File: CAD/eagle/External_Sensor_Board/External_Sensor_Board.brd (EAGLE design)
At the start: 50.8 x 43.4 mm, 14 parts, among them J1 SFW15R_FFC, J2 J30J-25, U1 MAX31725MTA+, U2 SSCMNNN015PA2A3, U3 P82B715

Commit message: Final layouts and gerbers
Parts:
- added U$1: SSL.3IN_SILK, images:SSL_SILK_.3IN
- added U$2: STAR, images:STAR_.3IN
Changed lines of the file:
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@@
 <?xml version="1.0" encoding="utf-8"?>
 <!DOCTYPE eagle SYSTEM "eagle.dtd">
-<eagle version="7.7.0">
+<eagle version="6.5.0">
 <drawing>
 <settings>
@@
 <layer number="2" name="Route2" color="1" fill="3" visible="no" active="yes"/>
 <layer number="3" name="Route3" color="4" fill="3" visible="no" active="yes"/>
+<layer number="4" name="Route4" color="1" fill="4" visible="no" active="yes"/>
+<layer number="5" name="Route5" color="4" fill="4" visible="no" active="yes"/>
+<layer number="6" name="Route6" color="1" fill="8" visible="no" active="yes"/>
+<layer number="7" name="Route7" color="4" fill="8" visible="no" active="yes"/>
+<layer number="8" name="Route8" color="1" fill="2" visible="no" active="yes"/>
+<layer number="9" name="Route9" color="4" fill="2" visible="no" active="yes"/>
+<layer number="10" name="Route10" color="1" fill="7" visible="no" active="yes"/>
+<layer number="11" name="Route11" color="4" fill="7" visible="no" active="yes"/>
+<layer number="12" name="Route12" color="1" fill="5" visible="no" active="yes"/>
+<layer number="13" name="Route13" color="4" fill="5" visible="no" active="yes"/>
 <layer number="14" name="Route14" color="1" fill="6" visible="no" active="yes"/>
 <layer number="15" name="Route15" color="4" fill="6" visible="no" active="yes"/>
@@
 <pass name="Default">
 <param name="RoutingGrid" value="50mil"/>
-<param name="AutoGrid" value="1"/>
-<param name="Efforts" value="0"/>
-<param name="TopRouterVariant" value="1"/>
 <param name="tpViaShape" value="round"/>
-<param name="PrefDir.1" value="a"/>
+<param name="PrefDir.1" value="|"/>
 <param name="PrefDir.2" value="0"/>
 <param name="PrefDir.3" value="0"/>
@@
 <param name="PrefDir.14" value="0"/>
 <param name="PrefDir.15" value="0"/>
-<param name="PrefDir.16" value="a"/>
+<param name="PrefDir.16" value="-"/>
 <param name="cfVia" value="8"/>
 <param name="cfNonPref" value="5"/>
@@
 <attribute name="NAME" x="2.0828" y="35.4584" size="0.8128" layer="25"/>
 </element>
+<element name="U$1" library="images" package="SSL_SILK_.3IN" value="SSL.3IN_SILK" x="46.99" y="5.08" rot="MR0"/>
+<element name="U$2" library="images" package="STAR_.3IN" value="STAR" x="11.43" y="5.08" rot="MR0"/>
 </elements>
 <signals>

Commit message: Beginning rework of expternal sensor board.
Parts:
- removed C2: 1uF, resistor:C0603
- removed C3: 100nF, resistor:C0603
- removed U3: P82B715, CM_IC:SO8
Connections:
- removed net SCL_BUFF: J2.25, U3.2
- removed net SDA_BUFF: J2.23, U3.7
- net +3V3: no longer C2.1, C3.1, U3.8
- net GND: no longer C2.2, C3.2, U3.4
- net SCL: now also J2.25; no longer U3.3
- net SDA: now also J2.23; no longer U3.6
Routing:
- net CAM_D0_P: track 57.9 -> 0.00 mm, vias 2 -> 0
- net CAM_D1_P: track 56.8 -> 0.00 mm, vias 1 -> 0
- net CAM_D0_N: track 56.2 -> 0.00 mm, vias 2 -> 0
- net CAM_D1_N: track 54.4 -> 0.00 mm, vias 1 -> 0
- net SDA_BUFF: track 53.5 -> 0.00 mm, vias 2 -> 0
- net SCL_BUFF: track 49.0 -> 0.00 mm, vias 2 -> 0
- net CAM_GND4: track 47.9 -> 0.00 mm, vias 1 -> 0
- net CAM_GPIO0: track 46.6 -> 0.00 mm, vias 1 -> 0
- net CAM_GPIO1: track 45.7 -> 0.00 mm, vias 1 -> 0
- net CAM_SCL: track 42.9 -> 0.00 mm, vias 1 -> 0
- net CAM_GND3: track 42.3 -> 0.00 mm, vias 1 -> 0
- net CAM_GND1: track 41.4 -> 0.00 mm, vias 1 -> 0
- net CAM_GND2: track 36.7 -> 0.00 mm, vias 1 -> 0
- net SDA: track 79.1 -> 113.4 mm
- net SCL: track 80.3 -> 108.9 mm
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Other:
- outline, holes or cut-outs redrawn
- board text added: "OPTIONAL"
- board text added: "REV 2 May 2017"
- board text removed: "REV 1.1 Feb. 2017"

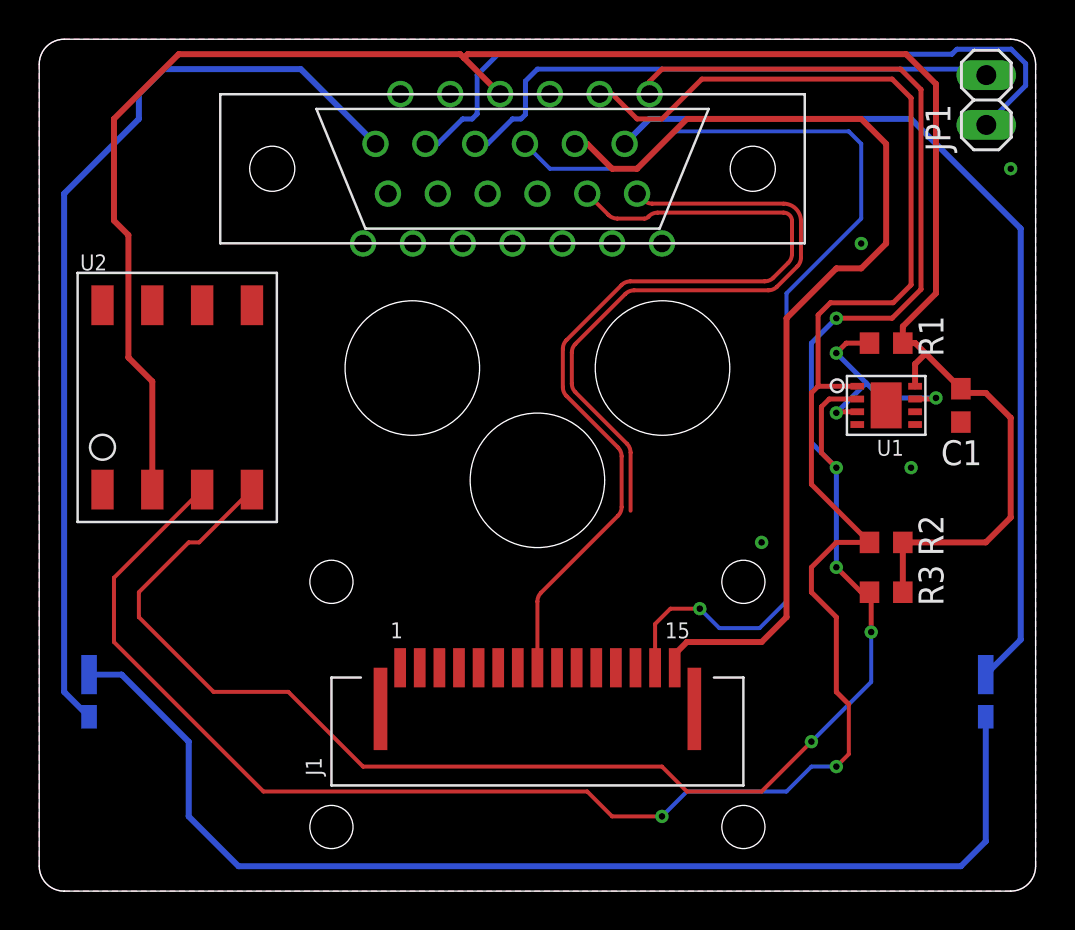
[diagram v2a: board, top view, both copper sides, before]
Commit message: Finished External Sensor Board reroute.
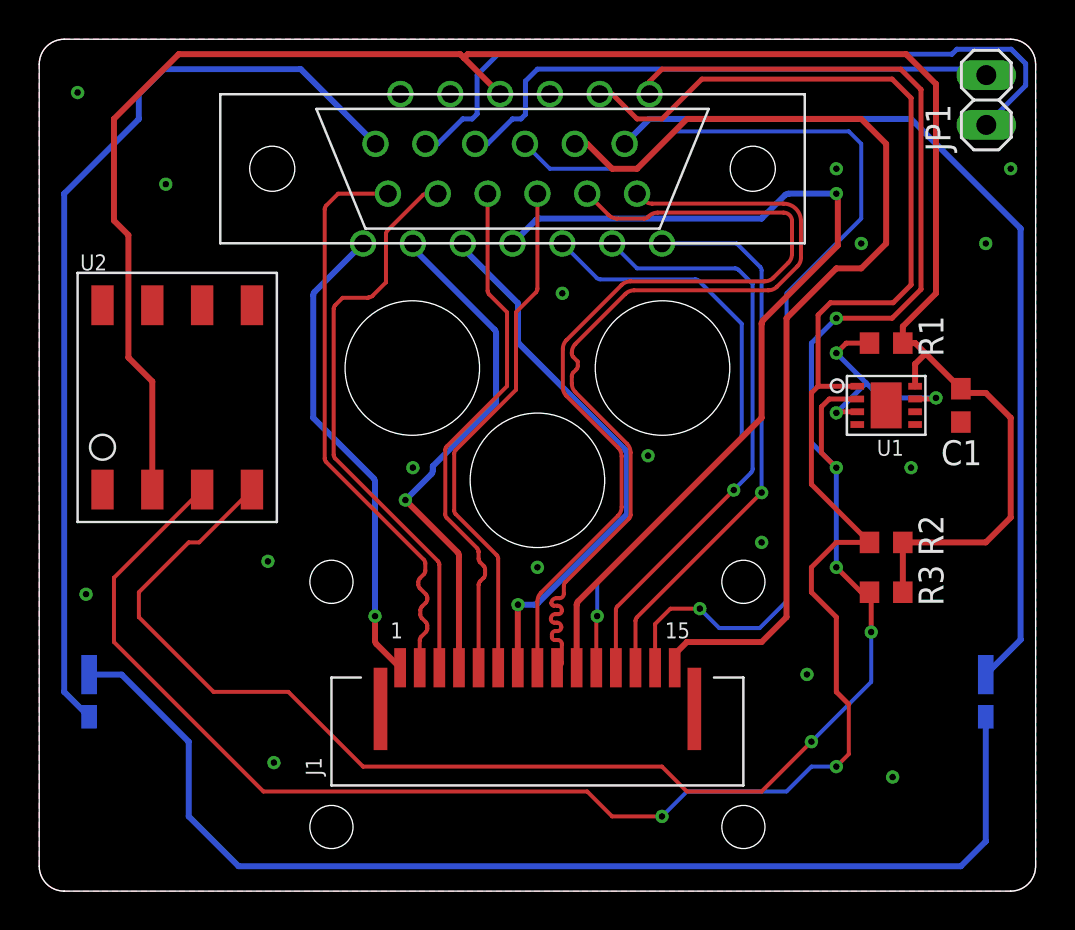
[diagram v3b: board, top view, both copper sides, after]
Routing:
- net CAM_GND4: track 0.00 -> 47.2 mm, vias 0 -> 1
- net CAM_GPIO0: track 0.00 -> 31.4 mm, vias 0 -> 1
- net CAM_GPIO1: track 0.00 -> 30.4 mm, vias 0 -> 1
- net CAM_D0_P: track 0.00 -> 29.7 mm
- net CAM_D0_N: track 0.00 -> 29.7 mm
- net CAM_SCL: track 0.00 -> 28.6 mm, vias 0 -> 1
- net CAM_GND3: track 0.00 -> 27.9 mm, vias 0 -> 1
- net CAM_D1_P: track 0.00 -> 26.8 mm
- net CAM_D1_N: track 0.00 -> 26.7 mm
- net CAM_GND2: track 0.00 -> 26.4 mm, vias 0 -> 1
- net CAM_GND1: track 0.00 -> 24.5 mm, vias 0 -> 1
- net CAM_C_P: track 33.8 -> 45.4 mm

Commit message: Minor changes to external board upon review.
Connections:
- removed net CAM_GND1: J1.1, J2.1
- removed net CAM_GND2: J1.4, J2.3
- removed net CAM_GND3: J1.7, J2.5
- removed net CAM_GND4: J1.10, J2.7
- net GND: now also J1.1, J1.10, J1.4, J1.7, J2.1, J2.3, J2.5, J2.7
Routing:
- net CAM_GND4: track 47.2 -> 0.00 mm, vias 1 -> 0
- net CAM_GND3: track 27.9 -> 0.00 mm, vias 1 -> 0
- net CAM_GND2: track 26.4 -> 0.00 mm, vias 1 -> 0
- net CAM_GND1: track 24.5 -> 0.00 mm, vias 1 -> 0
- net CAM_GPIO0: track 31.4 -> 23.2 mm
- net CAM_D0_P: track 29.7 -> 30.8 mm
- net CAM_D0_N: track 29.7 -> 30.4 mm

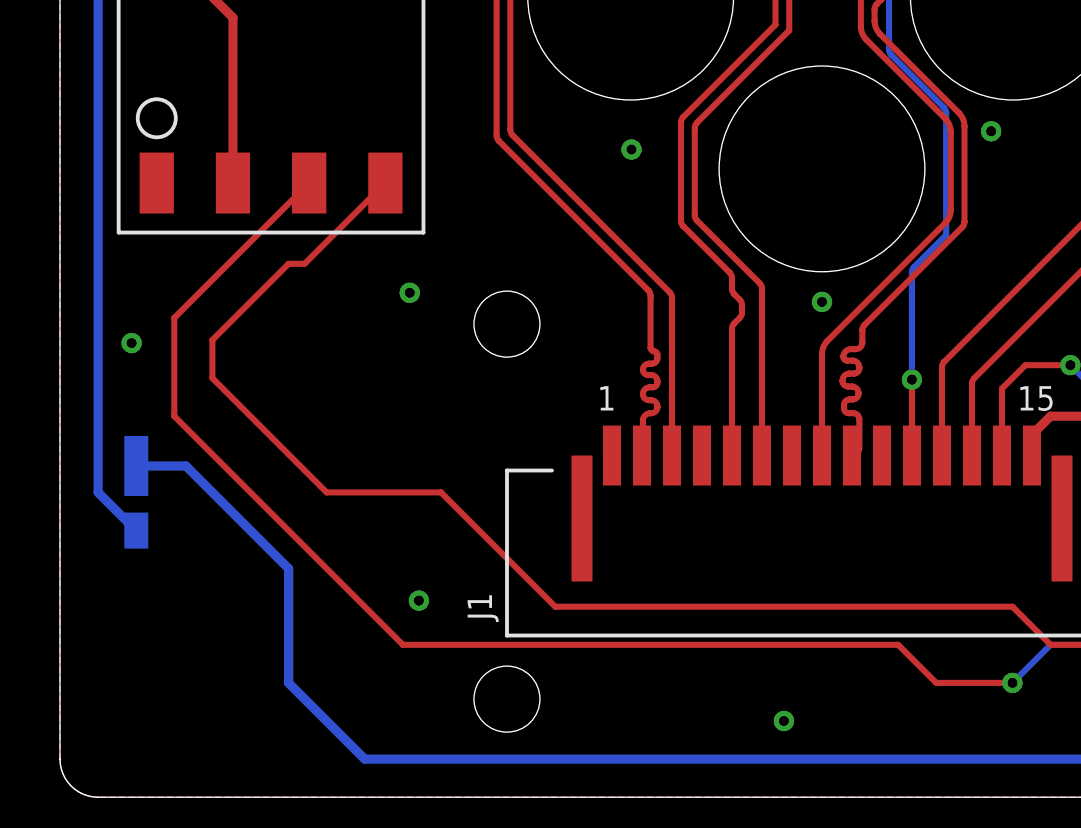
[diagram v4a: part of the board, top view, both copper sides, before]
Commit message: ESB traces and breakout 15 pin labels
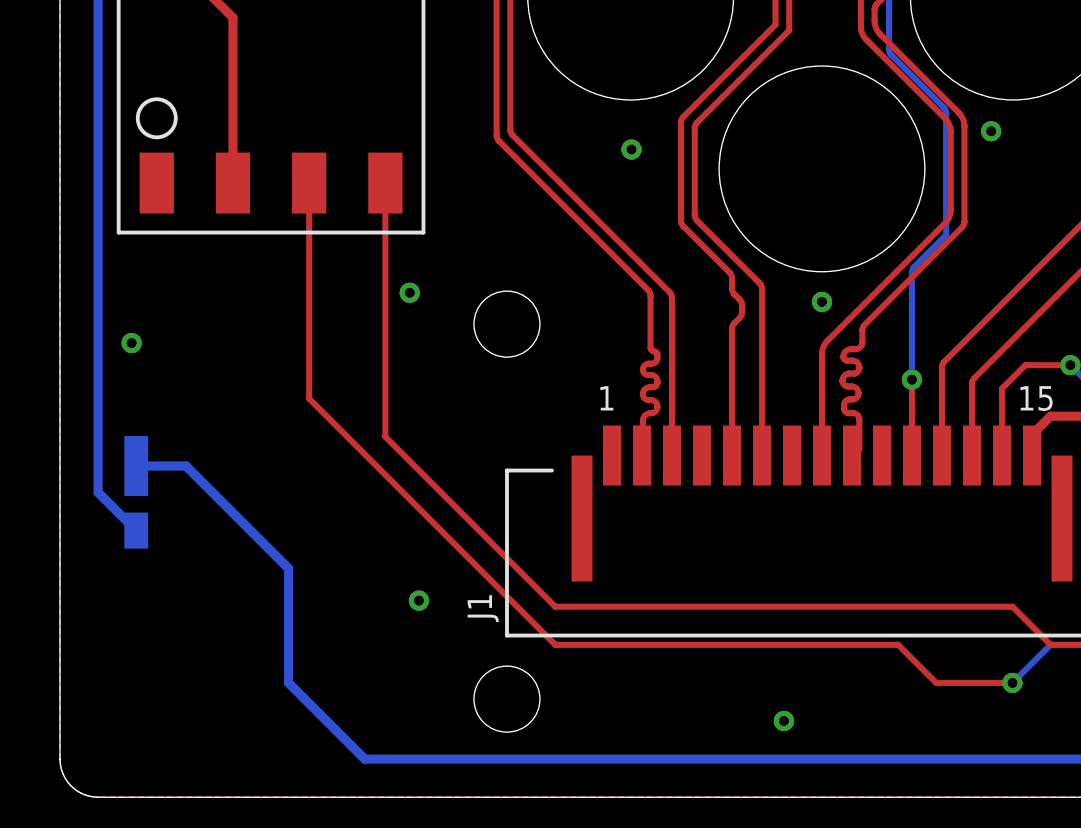
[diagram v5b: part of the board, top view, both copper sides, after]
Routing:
- net SCL: track 108.9 -> 101.6 mm
- net SDA: track 113.4 -> 106.7 mm
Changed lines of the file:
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@@
 <?xml version="1.0" encoding="utf-8"?>
 <!DOCTYPE eagle SYSTEM "eagle.dtd">
-<eagle version="7.7.0">
+<eagle version="6.5.0">
 <drawing>
 <settings>
@@
 <pass name="Default">
 <param name="RoutingGrid" value="50mil"/>
-<param name="AutoGrid" value="1"/>
-<param name="Efforts" value="0"/>
-<param name="TopRouterVariant" value="1"/>
 <param name="tpViaShape" value="round"/>
 <param name="PrefDir.1" value="|"/>
@@
 <wire x1="40.64" y1="21.59" x2="42.33" y2="21.59" width="0.254" layer="1"/>
 <contactref element="U2" pad="3"/>
-<wire x1="8.3058" y1="24.2824" x2="3.81" y2="19.7866" width="0.2032" layer="1"/>
-<wire x1="3.81" y1="19.7866" x2="3.81" y2="16.51" width="0.2032" layer="1"/>
-<wire x1="3.81" y1="16.51" x2="11.43" y2="8.89" width="0.2032" layer="1"/>
-<wire x1="11.43" y1="8.89" x2="27.94" y2="8.89" width="0.2032" layer="1"/>
 <wire x1="27.94" y1="8.89" x2="29.21" y2="7.62" width="0.2032" layer="1"/>
 <wire x1="29.21" y1="7.62" x2="31.75" y2="7.62" width="0.2032" layer="1"/>
@@
 <wire x1="44.45" y1="44.2468" x2="43.4848" y2="45.212" width="0.254" layer="1"/>
 <wire x1="43.4848" y1="45.212" x2="33.782" y2="45.212" width="0.254" layer="1"/>
+<wire x1="27.94" y1="8.89" x2="16.51" y2="8.89" width="0.2032" layer="1"/>
+<wire x1="16.51" y1="8.89" x2="8.3058" y2="17.0942" width="0.2032" layer="1"/>
+<wire x1="8.3058" y1="17.0942" x2="8.3058" y2="24.2824" width="0.2032" layer="1"/>
 </signal>
 <signal name="SCL">
@@
 <wire x1="42.418" y1="18.962" x2="42.33" y2="19.05" width="0.254" layer="1"/>
 <contactref element="U2" pad="4"/>
-<wire x1="10.8458" y1="24.2824" x2="8.1534" y2="21.59" width="0.2032" layer="1"/>
-<wire x1="8.1534" y1="21.59" x2="7.62" y2="21.59" width="0.2032" layer="1"/>
-<wire x1="7.62" y1="21.59" x2="5.08" y2="19.05" width="0.2032" layer="1"/>
-<wire x1="5.08" y1="19.05" x2="5.08" y2="17.78" width="0.2032" layer="1"/>
-<wire x1="5.08" y1="17.78" x2="8.89" y2="13.97" width="0.2032" layer="1"/>
-<wire x1="8.89" y1="13.97" x2="12.7" y2="13.97" width="0.2032" layer="1"/>
-<wire x1="12.7" y1="13.97" x2="16.51" y2="10.16" width="0.2032" layer="1"/>
+<wire x1="10.8458" y1="15.8242" x2="16.51" y2="10.16" width="0.2032" layer="1"/>
 <wire x1="16.51" y1="10.16" x2="31.75" y2="10.16" width="0.2032" layer="1"/>
 <wire x1="31.75" y1="10.16" x2="33.02" y2="8.89" width="0.2032" layer="1"/>
@@
 <wire x1="39.37" y1="11.43" x2="42.418" y2="14.478" width="0.2032" layer="16"/>
 <wire x1="42.418" y1="14.478" x2="42.418" y2="17.018" width="0.2032" layer="16"/>
+<wire x1="10.8458" y1="15.8242" x2="10.8458" y2="24.2824" width="0.2032" layer="1"/>
 </signal>
 <signal name="N$1">
